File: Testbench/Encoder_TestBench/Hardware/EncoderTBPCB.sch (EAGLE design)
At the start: 16 parts, among them IC1 7805DT, Q1 16MHz, U1 ATMEGA328P-PU, X1 C-GRID-05-15-91

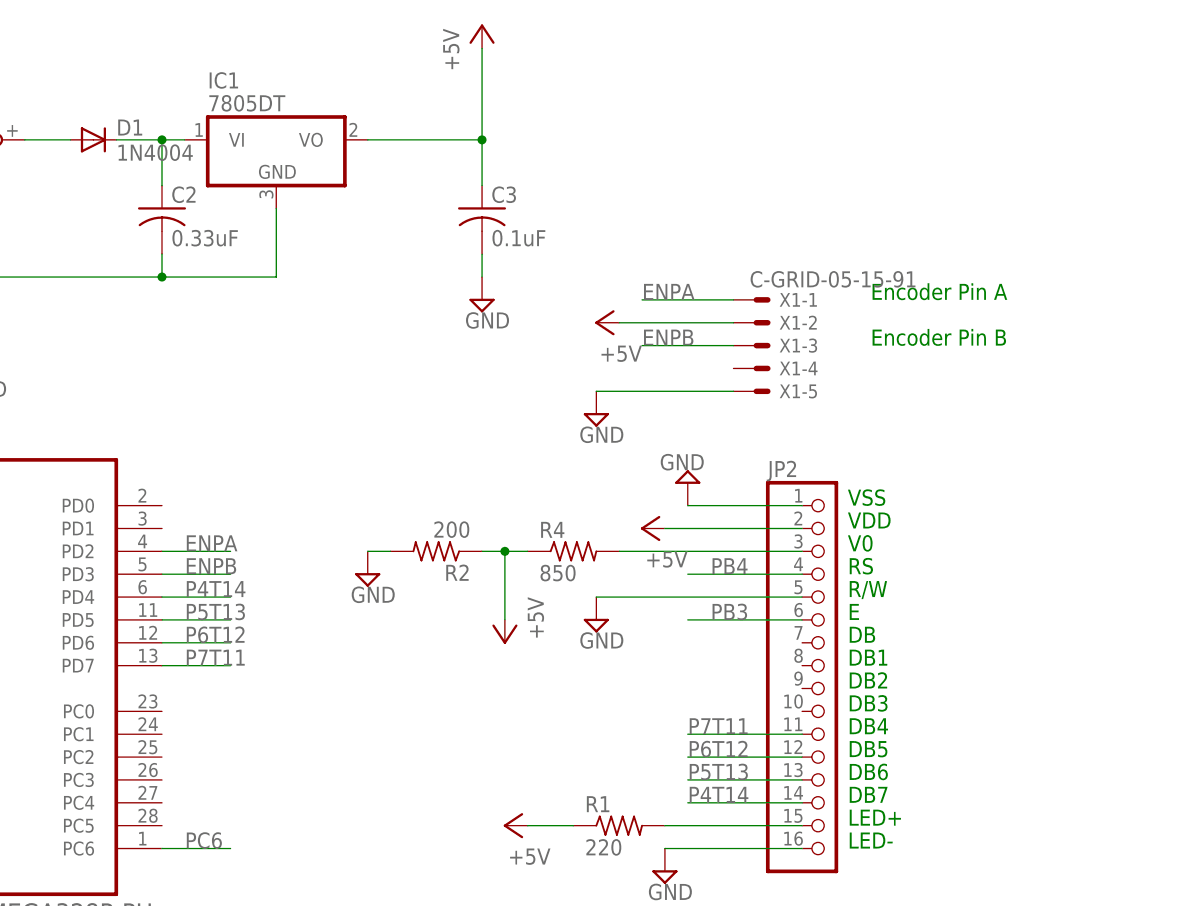
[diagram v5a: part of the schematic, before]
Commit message: Serial Communication Connector Added
Thanks @2Ryan09 for pointing that out.
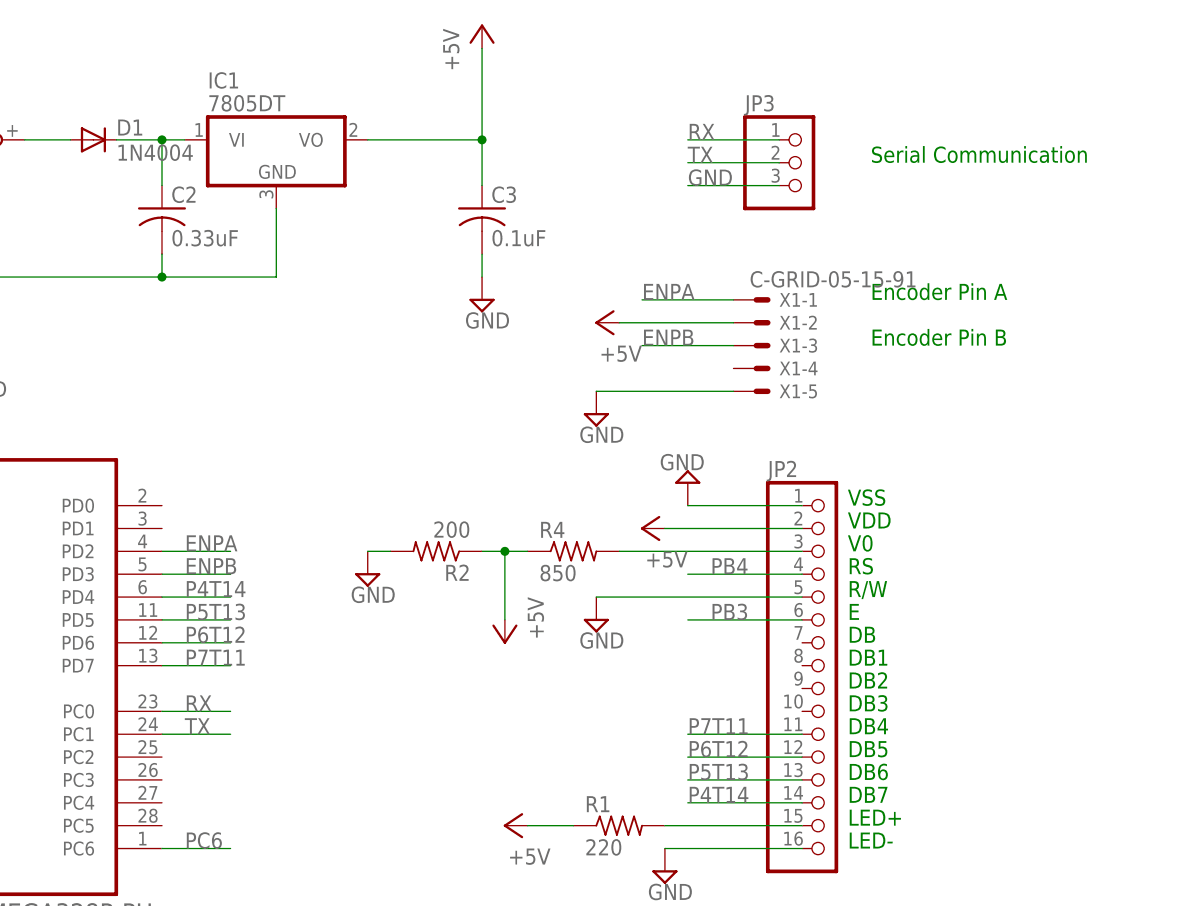
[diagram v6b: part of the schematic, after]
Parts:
- added JP3: (no value), pinhead:PINHD-1X3
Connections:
- new net RX: JP3.1, U1.PC0
- new net TX: JP3.2, U1.PC1
- net GND: now also JP3.3
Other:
- note added: "Serial Communication"
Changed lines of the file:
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@@
 <part name="SUPPLY11" library="supply2" deviceset="GND" device=""/>
 <part name="P+7" library="supply1" deviceset="+5V" device=""/>
+<part name="JP3" library="pinhead" deviceset="PINHD-1X3" device=""/>
 </parts>
 <sheets>
@@
 <text x="96.52" y="38.1" size="1.778" layer="91">Encoder Pin A</text>
 <text x="96.52" y="33.02" size="1.778" layer="91">Encoder Pin B</text>
+<text x="96.52" y="53.34" size="1.778" layer="91">Serial Communication</text>
 </plain>
 <instances>
@@
 <instance part="SUPPLY11" gate="GND" x="63.5" y="-43.18"/>
 <instance part="P+7" gate="1" x="66.04" y="-35.56" rot="R270"/>
+<instance part="JP3" gate="A" x="88.9" y="53.34"/>
 </instances>
 <busses>
@@
 <wire x1="-66.04" y1="-7.62" x2="-68.58" y2="-7.62" width="0.1524" layer="91"/>
 </segment>
+<segment>
+<pinref part="JP3" gate="A" pin="3"/>
+<wire x1="86.36" y1="50.8" x2="76.2" y2="50.8" width="0.1524" layer="91"/>
+<label x="76.2" y="50.8" size="1.778" layer="95"/>
+</segment>
 </net>
 <net name="P7T11" class="0">
@@
 </segment>
 </net>
+<net name="RX" class="0">
+<segment>
+<pinref part="JP3" gate="A" pin="1"/>
+<wire x1="86.36" y1="55.88" x2="76.2" y2="55.88" width="0.1524" layer="91"/>
+<label x="76.2" y="55.88" size="1.778" layer="95"/>
+</segment>
+<segment>
+<pinref part="U1" gate="A" pin="PC0"/>
+<wire x1="17.78" y1="-7.62" x2="25.4" y2="-7.62" width="0.1524" layer="91"/>
+<label x="20.32" y="-7.62" size="1.778" layer="95"/>
+</segment>
+</net>
+<net name="TX" class="0">
+<segment>
+<pinref part="JP3" gate="A" pin="2"/>
+<wire x1="86.36" y1="53.34" x2="76.2" y2="53.34" width="0.1524" layer="91"/>
+<label x="76.2" y="53.34" size="1.778" layer="95"/>
+</segment>
+<segment>
+<pinref part="U1" gate="A" pin="PC1"/>
+<wire x1="17.78" y1="-10.16" x2="25.4" y2="-10.16" width="0.1524" layer="91"/>
+<label x="20.32" y="-10.16" size="1.778" layer="95"/>
+</segment>
+</net>

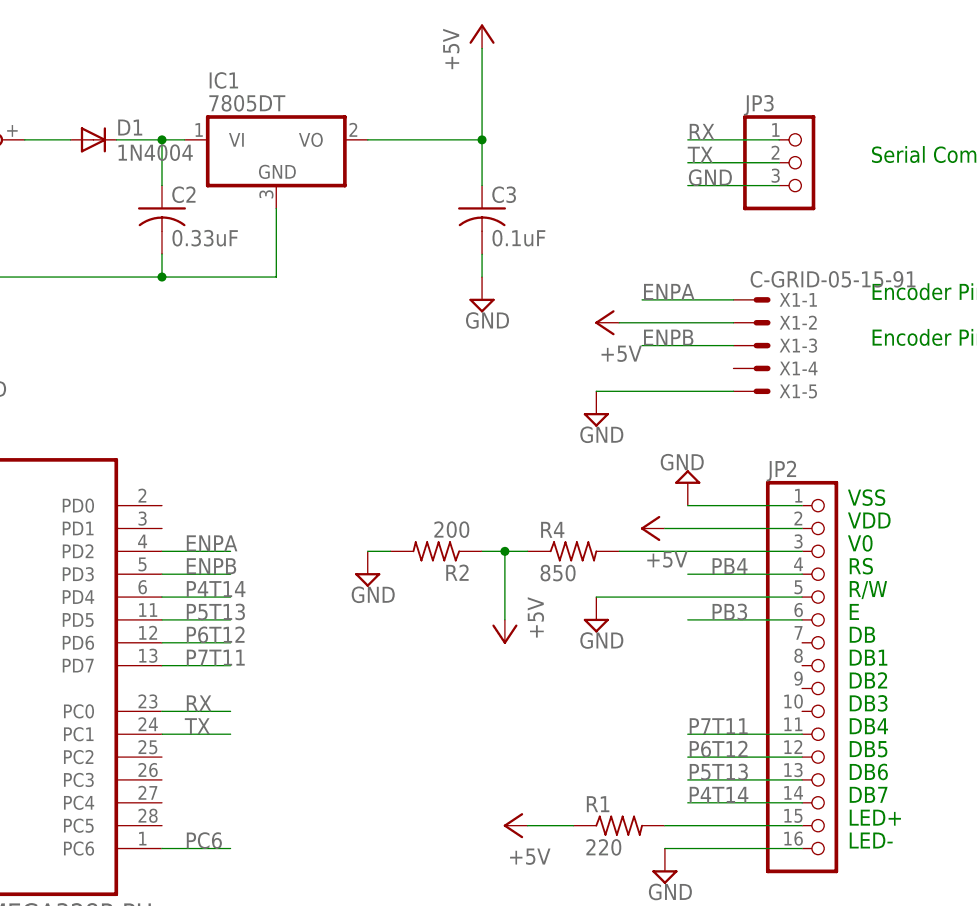
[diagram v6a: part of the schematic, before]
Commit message: Design Updated with 4 - pin Serial Connector
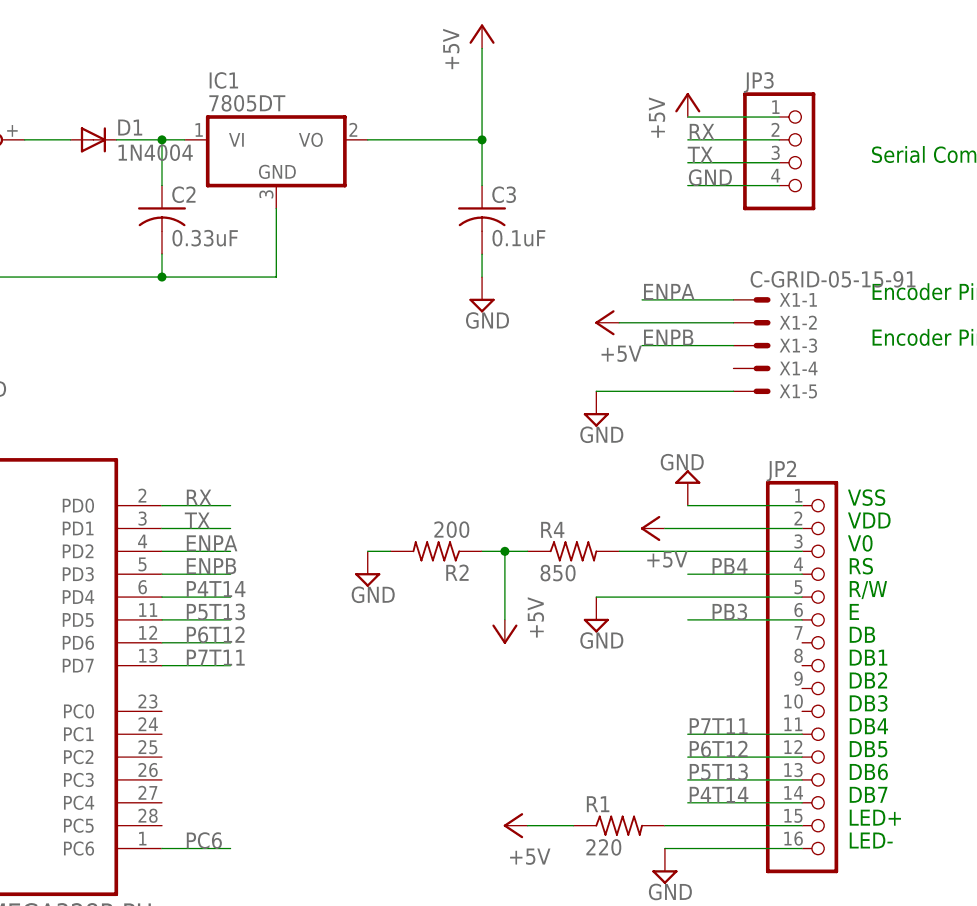
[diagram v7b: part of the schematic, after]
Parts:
- JP3: device pinhead:PINHD-1X3 -> pinhead:PINHD-1X4
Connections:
- net GND: now also JP3.4; no longer JP3.3
- net RX: now also JP3.2, U1.PD0; no longer JP3.1, U1.PC0
- net TX: now also JP3.3, U1.PD1; no longer JP3.2, U1.PC1
- net VDD: now also JP3.1
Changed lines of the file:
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@@
 <part name="SUPPLY11" library="supply2" deviceset="GND" device=""/>
 <part name="P+7" library="supply1" deviceset="+5V" device=""/>
-<part name="JP3" library="pinhead" deviceset="PINHD-1X3" device=""/>
+<part name="JP3" library="pinhead" deviceset="PINHD-1X4" device=""/>
+<part name="P+8" library="supply1" deviceset="+5V" device=""/>
 </parts>
 <sheets>
@@
 <instance part="P+7" gate="1" x="66.04" y="-35.56" rot="R270"/>
 <instance part="JP3" gate="A" x="88.9" y="53.34"/>
+<instance part="P+8" gate="1" x="76.2" y="60.96"/>
 </instances>
 <busses>
@@
 <wire x1="53.34" y1="-35.56" x2="63.5" y2="-35.56" width="0.1524" layer="91"/>
 <pinref part="P+7" gate="1" pin="+5V"/>
+</segment>
+<segment>
+<pinref part="JP3" gate="A" pin="1"/>
+<wire x1="86.36" y1="58.42" x2="76.2" y2="58.42" width="0.1524" layer="91"/>
+<pinref part="P+8" gate="1" pin="+5V"/>
 </segment>
 </net>
@@
 </segment>
 <segment>
-<pinref part="JP3" gate="A" pin="3"/>
 <wire x1="86.36" y1="50.8" x2="76.2" y2="50.8" width="0.1524" layer="91"/>
 <label x="76.2" y="50.8" size="1.778" layer="95"/>
+<pinref part="JP3" gate="A" pin="4"/>
 </segment>
 </net>
@@
 <net name="RX" class="0">
 <segment>
-<pinref part="JP3" gate="A" pin="1"/>
 <wire x1="86.36" y1="55.88" x2="76.2" y2="55.88" width="0.1524" layer="91"/>
 <label x="76.2" y="55.88" size="1.778" layer="95"/>
-</segment>
-<segment>
-<pinref part="U1" gate="A" pin="PC0"/>
-<wire x1="17.78" y1="-7.62" x2="25.4" y2="-7.62" width="0.1524" layer="91"/>
-<label x="20.32" y="-7.62" size="1.778" layer="95"/>
+<pinref part="JP3" gate="A" pin="2"/>
+</segment>
+<segment>
+<pinref part="U1" gate="A" pin="PD0"/>
+<wire x1="17.78" y1="15.24" x2="25.4" y2="15.24" width="0.1524" layer="91"/>
+<label x="20.32" y="15.24" size="1.778" layer="95"/>
 </segment>
 </net>
 <net name="TX" class="0">
 <segment>
-<pinref part="JP3" gate="A" pin="2"/>
 <wire x1="86.36" y1="53.34" x2="76.2" y2="53.34" width="0.1524" layer="91"/>
 <label x="76.2" y="53.34" size="1.778" layer="95"/>
-</segment>
-<segment>
-<pinref part="U1" gate="A" pin="PC1"/>
-<wire x1="17.78" y1="-10.16" x2="25.4" y2="-10.16" width="0.1524" layer="91"/>
-<label x="20.32" y="-10.16" size="1.778" layer="95"/>
-</segment>
-</net>
+<pinref part="JP3" gate="A" pin="3"/>
+</segment>
+<segment>
+<pinref part="U1" gate="A" pin="PD1"/>
+<wire x1="17.78" y1="12.7" x2="25.4" y2="12.7" width="0.1524" layer="91"/>
+<label x="20.32" y="12.7" size="1.778" layer="95"/>
+</segment>
+</net>
